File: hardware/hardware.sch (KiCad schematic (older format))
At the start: 4 parts

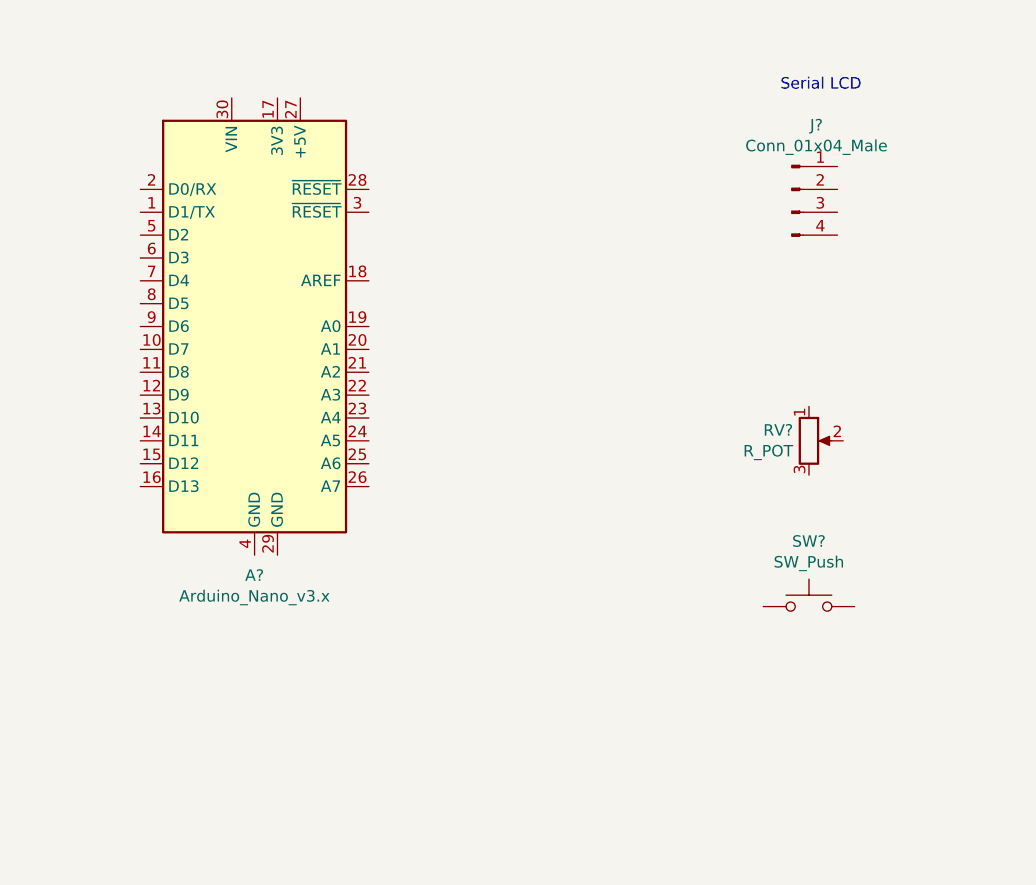
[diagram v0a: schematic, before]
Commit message: Output button state, draw breadboard schematic
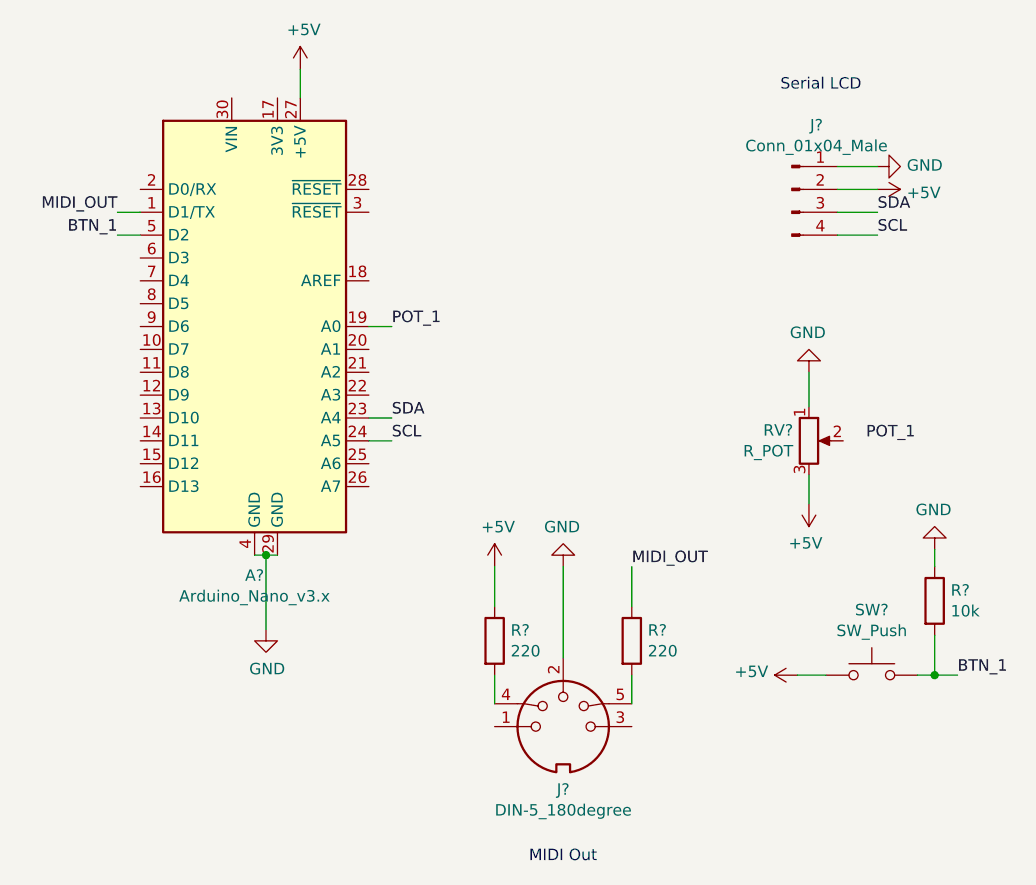
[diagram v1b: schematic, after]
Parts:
- added J?: DIN-5_180degree, symbol Connector:DIN-5_180degree
- added R? (x2): 220, symbol Device:R
- added R?: 10k, symbol Device:R
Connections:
- net MIDI_OUT: now reaches A?.1 (D1/TX)
- net MIDI_OUT: now also R?.1
- net POT_1: now reaches A?.19 (A0)
- net SDA: now reaches A?.23 (A4)
- net SDA: now also J?.3 (Pin_3)
- net SCL: now reaches A?.24 (A5)
- net SCL: now also J?.4 (Pin_4)
- net +5V: now reaches A?.27 (+5V)
- net +5V: now also J?.2 (Pin_2), RV?.3, SW?.1, R?.1
- net GND: now reaches A?.29 (GND)
- net GND: now also A?.4 (GND), J?.1 (Pin_1), RV?.1, J?.2, R?.1
- net BTN_1: now reaches A?.5 (D2)
- net BTN_1: now also SW?.2, R?.2
- new net: J?.4, R?.2
- new net: J?.5, R?.2
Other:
- note added: "MIDI Out"
- moved on the sheet: SW?
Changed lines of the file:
@@
 L Switch:SW_Push SW?
 U 1 1 5FC52801
-P 7500 3975
-F 0 "SW?" H 7500 4260 50  0000 C CNN
-F 1 "SW_Push" H 7500 4169 50  0000 C CNN
-F 2 "" H 7500 4175 50  0001 C CNN
-F 3 "~" H 7500 4175 50  0001 C CNN
-	1    7500 3975
-	1    0    0    -1
-$EndComp
+P 7775 4275
+F 0 "SW?" H 7775 4560 50  0000 C CNN
+F 1 "SW_Push" H 7775 4469 50  0000 C CNN
+F 2 "" H 7775 4475 50  0001 C CNN
+F 3 "~" H 7775 4475 50  0001 C CNN
+	1    7775 4275
+	1    0    0    -1
+$EndComp
+$Comp
+L Connector:DIN-5_180degree J?
+U 1 1 5FC510B6
+P 6425 4500
+F 0 "J?" H 6425 4225 50  0000 C CNN
+F 1 "DIN-5_180degree" H 6425 4134 50  0000 C CNN
+F 2 "" H 6425 4500 50  0001 C CNN
+F 3 "http://www.mouser.com/ds/2/18/40_c091_abd_e-75918.pdf" H 6425 4500 50  0001 C CNN
+	1    6425 4500
+	1    0    0    -1
+$EndComp
+Text Notes 6275 5100 0    50   ~ 0
+MIDI Out
+$Comp
+L Device:R R?
+U 1 1 5FC57B2D
+P 6125 4125
+F 0 "R?" H 6195 4171 50  0000 L CNN
+F 1 "220" H 6195 4080 50  0000 L CNN
+F 2 "" V 6055 4125 50  0001 C CNN
+F 3 "~" H 6125 4125 50  0001 C CNN
+	1    6125 4125
+	1    0    0    -1
+$EndComp
+$Comp
+L Device:R R?
+U 1 1 5FC580C5
+P 6725 4125
+F 0 "R?" H 6795 4171 50  0000 L CNN
+F 1 "220" H 6795 4080 50  0000 L CNN
+F 2 "" V 6655 4125 50  0001 C CNN
+F 3 "~" H 6725 4125 50  0001 C CNN
+	1    6725 4125
+	1    0    0    -1
+$EndComp
+$Comp
+L power:+5V #PWR?
+U 1 1 5FC582B6
+P 6125 3800
+F 0 "#PWR?" H 6125 3650 50  0001 C CNN
+F 1 "+5V" H 6140 3973 50  0000 C CNN
+F 2 "" H 6125 3800 50  0001 C CNN
+F 3 "" H 6125 3800 50  0001 C CNN
+	1    6125 3800
+	1    0    0    -1
+$EndComp
+Text Label 6725 3800 0    50   ~ 0
+MIDI_OUT
+Wire Wire Line
+	6125 4400 6125 4275
+Wire Wire Line
+	6125 3800 6125 3975
+$Comp
+L power:GND #PWR?
+U 1 1 5FC58907
+P 6425 3800
+F 0 "#PWR?" H 6425 3550 50  0001 C CNN
+F 1 "GND" H 6430 3627 50  0000 C CNN
+F 2 "" H 6425 3800 50  0001 C CNN
+F 3 "" H 6425 3800 50  0001 C CNN
+	1    6425 3800
+	-1   0    0    1
+$EndComp
+Wire Wire Line
+	6425 3800 6425 4200
+Wire Wire Line
+	6725 3975 6725 3800
+Wire Wire Line
+	6725 4275 6725 4400
+Text Label 7800 2250 0    50   ~ 0
+SDA
+Text Label 7800 2350 0    50   ~ 0
+SCL
+$Comp
+L power:GND #PWR?
+U 1 1 5FC59421
+P 7800 2050
+F 0 "#PWR?" H 7800 1800 50  0001 C CNN
+F 1 "GND" V 7805 1922 50  0000 R CNN
+F 2 "" H 7800 2050 50  0001 C CNN
+F 3 "" H 7800 2050 50  0001 C CNN
+	1    7800 2050
+	0    -1   -1   0
+$EndComp
+$Comp
+L power:+5V #PWR?
+U 1 1 5FC5961D
+P 7800 2150
+F 0 "#PWR?" H 7800 2000 50  0001 C CNN
+F 1 "+5V" V 7815 2278 50  0000 L CNN
+F 2 "" H 7800 2150 50  0001 C CNN
+F 3 "" H 7800 2150 50  0001 C CNN
+	1    7800 2150
+	0    1    1    0
+$EndComp
+Wire Wire Line
+	7625 2050 7800 2050
+Wire Wire Line
+	7800 2150 7625 2150
+Wire Wire Line
+	7800 2250 7625 2250
+Wire Wire Line
+	7800 2350 7625 2350
+Text Label 5675 3150 0    50   ~ 0
+SDA
+Text Label 5675 3250 0    50   ~ 0
+SCL
+$Comp
+L power:GND #PWR?
+U 1 1 5FC5A30C
+P 5125 4075
+F 0 "#PWR?" H 5125 3825 50  0001 C CNN
+F 1 "GND" H 5130 3902 50  0000 C CNN
+F 2 "" H 5125 4075 50  0001 C CNN
+F 3 "" H 5125 4075 50  0001 C CNN
+	1    5125 4075
+	1    0    0    -1
+$EndComp
+$Comp
+L power:+5V #PWR?
+U 1 1 5FC5A4E2
+P 5275 1625
+F 0 "#PWR?" H 5275 1475 50  0001 C CNN
+F 1 "+5V" H 5290 1798 50  0000 C CNN
+F 2 "" H 5275 1625 50  0001 C CNN
+F 3 "" H 5275 1625 50  0001 C CNN
+	1    5275 1625
+	1    0    0    -1
+$EndComp
+Wire Wire Line
+	5275 1625 5275 1750
+Wire Wire Line
+	5075 3750 5125 3750
+Wire Wire Line
+	5125 4075 5125 3750
+Connection ~ 5125 3750
+Wire Wire Line
+	5125 3750 5175 3750
+Wire Wire Line
+	5575 3250 5675 3250
+Wire Wire Line
+	5575 3150 5675 3150
+Text Label 4475 2250 2    50   ~ 0
+MIDI_OUT
+Wire Wire Line
+	4475 2250 4575 2250
+Text Label 5675 2750 0    50   ~ 0
+POT_1
+Text Label 4475 2350 2    50   ~ 0
+BTN_1
+Wire Wire Line
+	5575 2750 5675 2750
+Wire Wire Line
+	4475 2350 4575 2350
+$Comp
+L power:GND #PWR?
+U 1 1 5FC5C0D4
+P 7500 2950
+F 0 "#PWR?" H 7500 2700 50  0001 C CNN
+F 1 "GND" H 7505 2777 50  0000 C CNN
+F 2 "" H 7500 2950 50  0001 C CNN
+F 3 "" H 7500 2950 50  0001 C CNN
+	1    7500 2950
+	-1   0    0    1
+$EndComp
+$Comp
+L power:+5V #PWR?
+U 1 1 5FC5C2F2
+P 7500 3525
+F 0 "#PWR?" H 7500 3375 50  0001 C CNN
+F 1 "+5V" H 7515 3698 50  0000 C CNN
+F 2 "" H 7500 3525 50  0001 C CNN
+F 3 "" H 7500 3525 50  0001 C CNN
+	1    7500 3525
+	-1   0    0    1
+$EndComp
+Wire Wire Line
+	7500 2950 7500 3100
+Wire Wire Line
+	7500 3400 7500 3525
+Text Label 7750 3250 0    50   ~ 0
+POT_1
+Text Label 8150 4275 0    50   ~ 0
+BTN_1
+$Comp
+L Device:R R?
+U 1 1 5FC5D15E
+P 8050 3950
+F 0 "R?" H 8120 3996 50  0000 L CNN
+F 1 "10k" H 8120 3905 50  0000 L CNN
+F 2 "" V 7980 3950 50  0001 C CNN
+F 3 "~" H 8050 3950 50  0001 C CNN
+	1    8050 3950
+	1    0    0    -1
+$EndComp
+$Comp
+L power:GND #PWR?
+U 1 1 5FC5D647
+P 8050 3725
+F 0 "#PWR?" H 8050 3475 50  0001 C CNN
+F 1 "GND" H 8055 3552 50  0000 C CNN
+F 2 "" H 8050 3725 50  0001 C CNN
+F 3 "" H 8050 3725 50  0001 C CNN
+	1    8050 3725
+	-1   0    0    1
+$EndComp
+$Comp
+L power:+5V #PWR?
+U 1 1 5FC5D891
+P 7450 4275
+F 0 "#PWR?" H 7450 4125 50  0001 C CNN
+F 1 "+5V" V 7465 4403 50  0000 L CNN
+F 2 "" H 7450 4275 50  0001 C CNN
+F 3 "" H 7450 4275 50  0001 C CNN
+	1    7450 4275
+	0    -1   -1   0
+$EndComp
+Wire Wire Line
+	8050 3725 8050 3800
+Wire Wire Line
+	7450 4275 7575 4275
+Wire Wire Line
+	8050 4100 8050 4275
+Wire Wire Line
+	7975 4275 8050 4275
+Connection ~ 8050 4275
+Wire Wire Line
+	8050 4275 8150 4275
 $EndSCHEMATC
